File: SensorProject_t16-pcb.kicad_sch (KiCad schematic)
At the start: 51 parts, among them J1 Conn_01x02_Pin, J10 Conn_01x02_Pin, J11 Conn_01x02_Pin, J12 Conn_01x02_Pin, J13 Conn_01x02_Pin, J14 Conn_01x02_Pin, J15 Conn_01x02_Pin, J16 Conn_01x02_Pin, J17 Conn_01x04_Socket, J2 Conn_01x02_Pin, J3 Conn_01x02_Pin, J4 Conn_01x02_Pin, J5 Conn_01x02_Pin, J6 Conn_01x02_Pin, J7 Conn_01x02_Pin, J8 Conn_01x02_Pin, J9 Conn_01x02_Pin, U1 ADS1115IDGS, U2 ADS1115IDGS, U3 ADS1115IDGS, U4 ADS1115IDGS

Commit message: As made,  t16-F411 v0.2.0 2025-05, with added notes about needed fixes and results from some testing.
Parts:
- C1, C2, C3, C4: Manufacturer (none) -> Samsung; MfgPart (none) -> CL10B104KB8NNNC
- R1, R10, R11, R12, R13, R14, R15, R16, R17, R18, R19, R2, R20, R21, R22, R3, R4, R5, R6, R7, R8, R9: Manufacturer (none) -> Vishay; MfgPart (none) -> CRCW060310K0FKEA

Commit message: Most post v0.2.0 fixes done. About to mess with GND_ANT zone and net.
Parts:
- added R31, R32: 10k 1%, ProjectLib:R_0603_1608Metric, symbol ProjectLib:R_US
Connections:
- net +3V3: now also R31.1, R32.2
- net SCL1: now also J17.3 (Pin_3), R31.2; no longer R17.2, U1.10 (SCL), U2.10 (SCL), U3.10 (SCL), U4.1 (ADDR), U4.10 (SCL)
- net SCL2: now also R17.2, U1.10 (SCL), U2.10 (SCL), U3.10 (SCL), U4.1 (ADDR), U4.10 (SCL); no longer J17.3 (Pin_3)
- net SDA1: now also J17.4 (Pin_4), R32.1; no longer R18.2, U1.9 (SDA), U2.9 (SDA), U3.1 (ADDR), U3.9 (SDA), U4.9 (SDA)
- net SDA2: now also R18.2, U1.9 (SDA), U2.9 (SDA), U3.1 (ADDR), U3.9 (SDA), U4.9 (SDA); no longer J17.4 (Pin_4)

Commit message: BOM cleaned up.
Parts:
- C1, C2, C3, C4: Notes (none) -> or equivalent; Package (none) -> C_0603_1608Metric
- J1, J10, J11, J12, J13, J14, J15, J16, J2, J3, J4, J5, J6, J7, J8, J9: Package (none) -> JST_XH_B2B-XH-A_1x02_P2.50mm_Vertical
- J17: Package (none) -> PinSocket_1x04_P2.54mm_Vertical
- R1, R10, R11, R12, R13, R14, R15, R16, R17, R18, R19, R2, R20, R21, R22, R3, R31, R32, R4, R5, R6, R7, R8, R9: Notes (none) -> or equivalent; Package (none) -> R_0603_1608Metric
- U1, U2, U3, U4: Notes (none) -> or equivalent; Package (none) -> TSSOP-10_3x3mm_P0.5mm

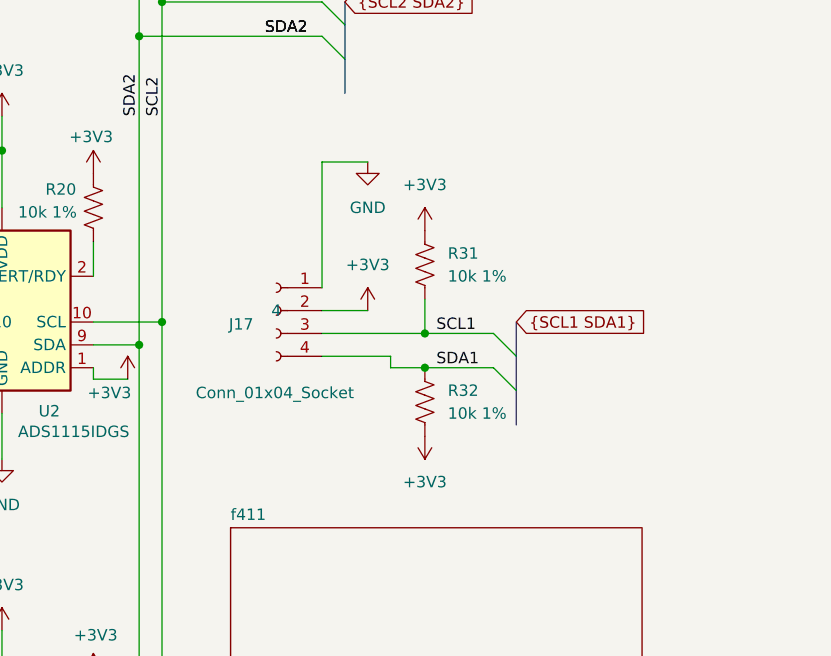
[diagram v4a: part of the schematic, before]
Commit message: flip side for radio in progress.
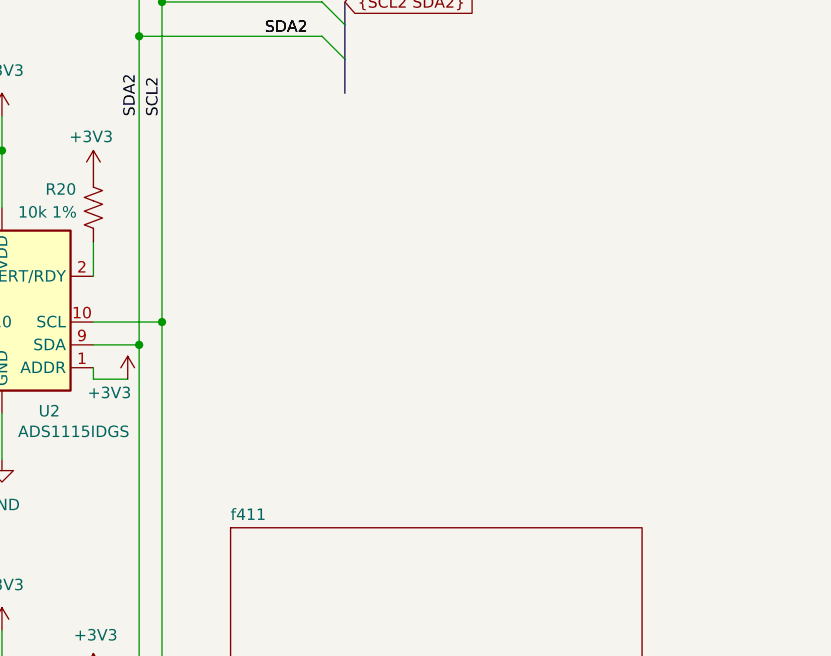
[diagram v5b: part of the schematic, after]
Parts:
- removed J17: Conn_01x04_Socket, ProjectLib:PinSocket_1x04_P2.54mm_Vertical, symbol ProjectLib:Conn_01x04_Socket
- removed R31, R32: 10k 1%, ProjectLib:R_0603_1608Metric, symbol ProjectLib:R_US

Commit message: converted R, C, and L to smaller 0402 footprints. Some trace rearranging and cleanup.
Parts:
- C1, C2, C3, C4: footprint ProjectLib:C_0603_1608Metric -> ProjectLib:C_0402_1005Metric; Manufacturer Samsung -> (none); MfgPart CL10B104KB8NNNC -> (none); Package C_0603_1608Metric -> C_0402_1005Metric
- R1, R10, R11, R12, R13, R14, R15, R16, R17, R18, R19, R2, R20, R21, R22, R3, R4, R5, R6, R7, R8, R9: footprint ProjectLib:R_0603_1608Metric -> ProjectLib:R_0402_1005Metric; Manufacturer Vishay -> (none); MfgPart CRCW060310K0FKEA -> (none); Package R_0603_1608Metric -> R_0402_1005Metric
